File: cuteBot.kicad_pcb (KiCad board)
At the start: 2 copper layers, 39.9 x 39.9 mm, 67 parts, among them P1 USB_A, P2 BAT+, P3 BAT-, P4 MOTOR_A, P5 MOTOR_B, P6 CONN_02X03, Q1 S8050, SW1 SW_SPDT, SW2 SW_Push, SW3 SW_Push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

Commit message: Serigrafía terminada
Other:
- board text added: "+"
- board text added: "-"
- board text added: "CuteBot"
- board text added: "David Matias"
- board text added: "www.frizzy.es"
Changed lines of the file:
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@@
   (general
     (thickness 1.6)
-    (drawings 12)
+    (drawings 17)
     (tracks 863)
     (zones 0)
@@
     (pad_to_paste_clearance -0.04)
     (aux_axis_origin 0 0)
-    (visible_elements FFFDFF7F)
+    (visible_elements FFFFFF7F)
     (pcbplotparams
       (layerselection 0x3ffff_80000001)
@@
       (effects (font (size 0.6096 0.6096) (thickness 0.127)))
     )
-    (fp_text value CONN_02X03 (at -2.54 4.7752) (layer F.SilkS)
+    (fp_text value CONN_02X03 (at -2.54 4.7752) (layer F.SilkS) hide
       (effects (font (size 0.4 0.4) (thickness 0.1)))
     )
@@
       (at (xyz 0 0 0))
       (scale (xyz 1 1 1))
+      (rotate (xyz 0 0 0))
+    )
+    (model ${KISYS3DMOD}/Housings_SOIC.3dshapes/SOIJ-8_5.3x5.3mm_Pitch1.27mm.wrl
+      (at (xyz 0 0 0))
+      (scale (xyz 0.8 0.9 0.8))
       (rotate (xyz 0 0 0))
     )
@@
       (effects (font (size 0.4 0.4) (thickness 0.1)) (justify mirror))
     )
-    (fp_text user %R (at 0 2.5 270) (layer B.Fab)
+    (fp_text user %R (at 0.127 0.127 270) (layer B.Fab)
       (effects (font (size 1 1) (thickness 0.15)) (justify mirror))
     )
@@
       (rotate (xyz 0 0 0))
     )
+    (model ${KISYS3DMOD}/Connectors_USB.3dshapes/USB_Micro-B_Molex_47346-0001.wrl
+      (at (xyz 0 0 0))
+      (scale (xyz 1 1 1))
+      (rotate (xyz 0 0 0))
+    )
   )
   (module Connectors_TestPoints:Test_Point_Pad_d1.0mm (layer B.Cu)
@@
     (tags "test point SMD pad")
     (attr virtual)
-    (fp_text reference P2 (at 0 1.448) (layer B.SilkS)
+    (fp_text reference P2 (at 0 1.448) (layer B.SilkS) hide
       (effects (font (size 1 1) (thickness 0.15)) (justify mirror))
     )
@@
     (tags "test point SMD pad")
     (attr virtual)
-    (fp_text reference P3 (at 0 1.448) (layer B.SilkS)
+    (fp_text reference P3 (at 0 1.448) (layer B.SilkS) hide
       (effects (font (size 1 1) (thickness 0.15)) (justify mirror))
     )
@@
     (tags "resistor 0603")
     (attr smd)
-    (fp_text reference R2 (at 0.9405 1.3335 270) (layer B.SilkS)
+    (fp_text reference R2 (at 1.004 1.397 270) (layer B.SilkS)
       (effects (font (size 1 1) (thickness 0.15)) (justify mirror))
     )
@@
     (tags "resistor 0603")
     (attr smd)
-    (fp_text reference R3 (at -0.9525 -0.8255 90) (layer B.SilkS)
+    (fp_text reference R3 (at 2.8575 -0.0635 90) (layer B.SilkS)
       (effects (font (size 1 1) (thickness 0.15)) (justify mirror))
     )
@@
     (pad 17 smd rect (at 0 0 90) (size 2.1 2.1) (layers B.Cu B.Paste B.Mask)
       (net 4 GND) (solder_paste_margin_ratio -0.2))
+    (model ${KISYS3DMOD}/Package_DFN_QFN.3dshapes/MLPQ-16-1EP_4x4mm_P0.65mm_EP2.8x2.8mm.step
+      (at (xyz 0 0 0))
+      (scale (xyz 1 1 1))
+      (rotate (xyz 0 0 0))
+    )
   )
   (module JDY-08:JDY-08 (layer B.Cu)
@@
       (effects (font (size 0.6096 0.6096) (thickness 0.127)))
     )
-    (fp_text value 16MHz (at 2.54 0 -180) (layer F.SilkS)
+    (fp_text value 16MHz (at 2.54 0 180) (layer F.SilkS) hide
       (effects (font (size 0.4 0.4) (thickness 0.1)))
     )
@@
     (pad 3 smd oval (at 1.19888 0 90) (size 0.44958 1.905) (layers F.Cu F.Paste F.Mask)
       (net 90 "Net-(U1-Pad16)") (solder_mask_margin 0.1016))
+    (model "${KISYS3DMOD}/Modelos 3D descargados/Oscilador.wrl"
+      (offset (xyz -1.6 0.7 0))
+      (scale (xyz 0.4 0.4 0.4))
+      (rotate (xyz -90 0 0))
+    )
   )
   (module TO_SOT_Packages_SMD:SOT-23 (layer B.Cu)
@@
       (effects (font (size 0.4 0.4) (thickness 0.1)) (justify mirror))
     )
-    (fp_text user %R (at 0.508 0.254 180) (layer B.Fab)
+    (fp_text user %R (at -0.0475 -0.0025 180) (layer B.Fab)
       (effects (font (size 0.5 0.5) (thickness 0.075)) (justify mirror))
     )
@@
     (pad 1 np_thru_hole circle (at 0 0) (size 3.2 3.2) (drill 3.2) (layers *.Cu *.Mask))
   )
+  (gr_text www.frizzy.es (at 139.954 118.3005) (layer F.SilkS)
+    (effects (font (size 0.7 0.7) (thickness 0.127)))
+  )
+  (gr_text CuteBot (at 147.193 151.638) (layer F.SilkS)
+    (effects (font (size 0.6 0.6) (thickness 0.127)))
+  )
+  (gr_text "David Matias" (at 128.143 151.638) (layer F.SilkS)
+    (effects (font (size 0.6 0.6) (thickness 0.127)))
+  )
+  (gr_text - (at 151.892 142.6845) (layer B.SilkS)
+    (effects (font (size 0.6 0.6) (thickness 0.127)))
+  )
+  (gr_text + (at 151.892 139.192) (layer B.SilkS)
+    (effects (font (size 0.6 0.6) (thickness 0.127)))
+  )
   (gr_line (start 156.21 135.636) (end 121.412 135.636) (layer Dwgs.User) (width 0.127))

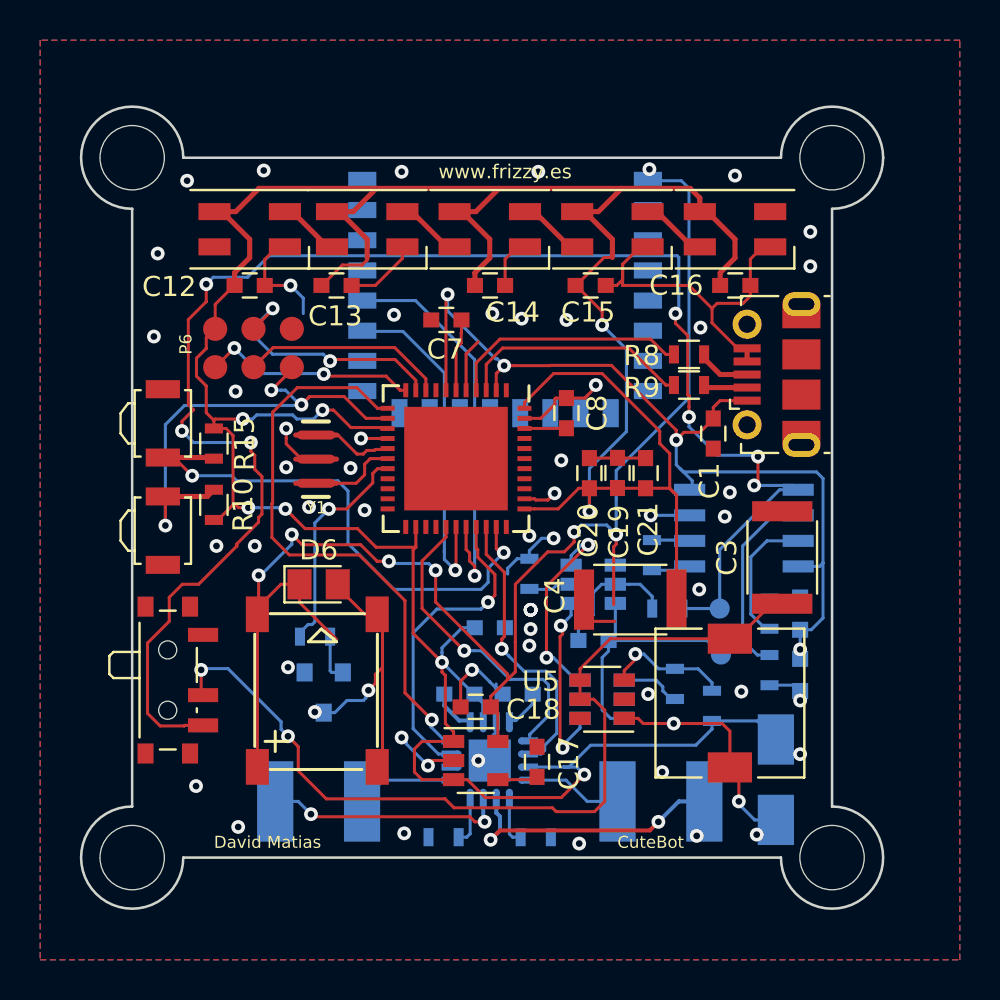
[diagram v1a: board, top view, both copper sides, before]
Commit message: Errores corregidos.
Vias que provocaban un corto, pinout del Q1 erróneo  y flag de los neopixel no conectado al micro.
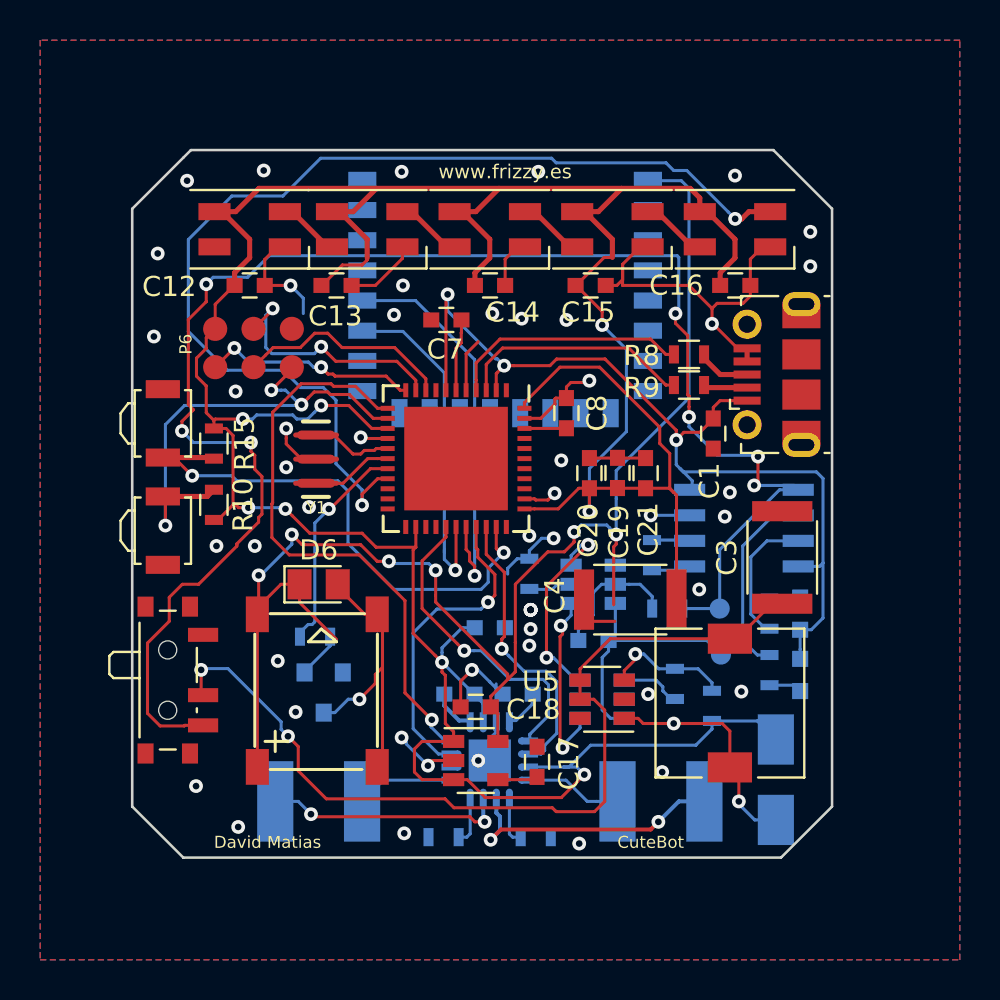
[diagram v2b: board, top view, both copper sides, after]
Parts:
- removed REF** (x4): MountingHole_3.2mm_M3, Mounting_Holes:MountingHole_3.2mm_M3
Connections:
- Q1 pad 1: GND -> Net-(Q1-Pad1)
- Q1 pad 2: Net-(Q1-Pad2) -> GND
- R16 pad 2: Net-(Q1-Pad2) -> Net-(Q1-Pad1)
- U1 pad 19: Net-(U1-Pad19) -> NEO
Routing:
- net NEO: track 0.00 -> 53.2 mm, vias 0 -> 2
- net Net-(Q1-Pad2): track 2.36 -> 0.00 mm
- net Net-(Q1-Pad1): track 0.00 -> 2.30 mm
- net SCK: track 10.2 -> 10.8 mm
- net 5V: track 179.0 -> 179.5 mm
- net GND: track 70.0 -> 70.2 mm, vias 55 -> 50
- net Vusb: track 47.1 -> 47.3 mm, vias 4 -> 3
- net Net-(P4-Pad2): vias 3 -> 2
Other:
- board size 39.9 x 39.9 mm -> 34.8 x 35.2 mm
